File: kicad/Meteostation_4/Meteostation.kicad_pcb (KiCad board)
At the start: 2 copper layers, 45 x 45 mm, 105 parts, among them J1 TxD, J10 GM+, J11 GM-, J12 SWD, J13 SWC, J2 RxD, J3 BME280_SCL, J4 BME280_SDA, J5 RST, J6 +EXT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

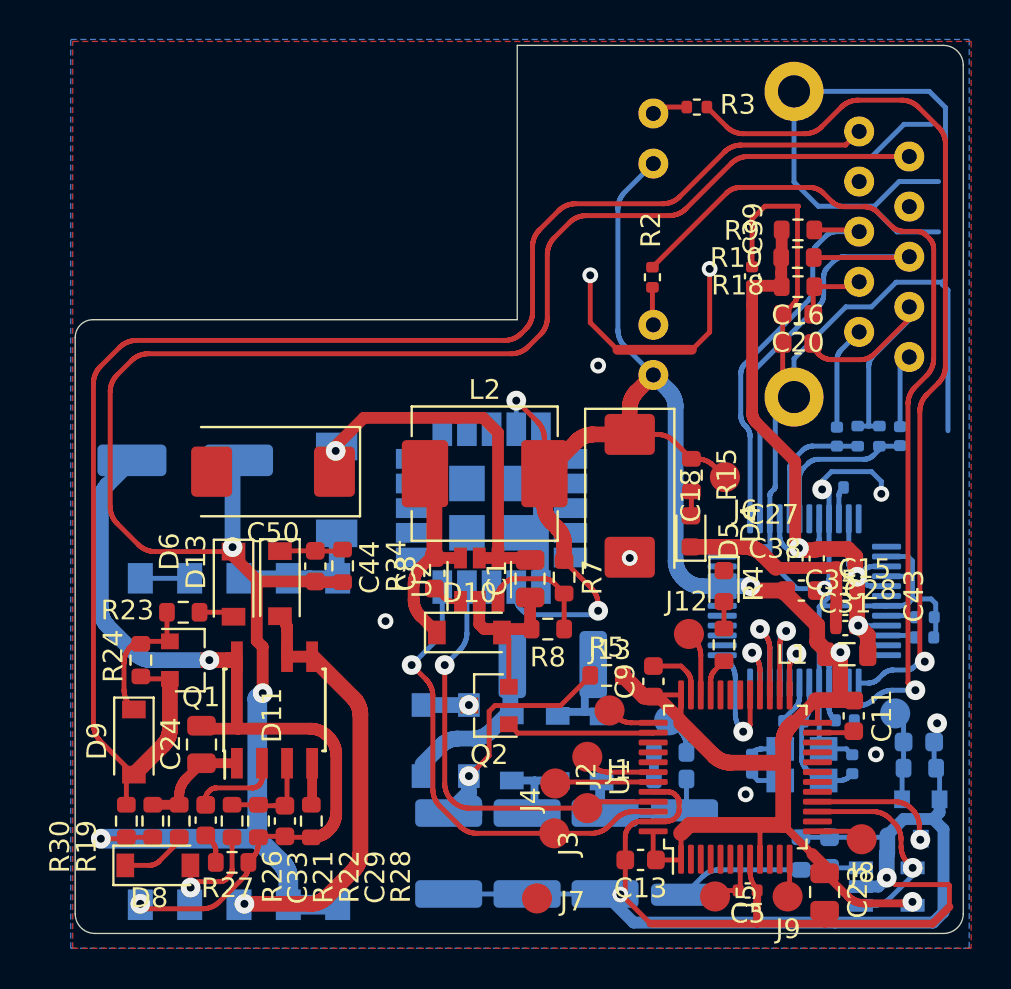
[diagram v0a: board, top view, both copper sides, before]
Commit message: новый файл:    Documents/5N10.pdf 	изменено:      kicad/Meteostation_4/Meteostation.kicad_pcb 	изменено:      kicad/Meteostation_4/Meteostation.kicad_pcb-bak 	изменено:      kicad/Meteostation_4/Meteostation.sch 	изменено:      kicad/Meteostation_4/Meteostation.sch-bak 	изменено:      kicad/Meteostation_4/fp-info-cache
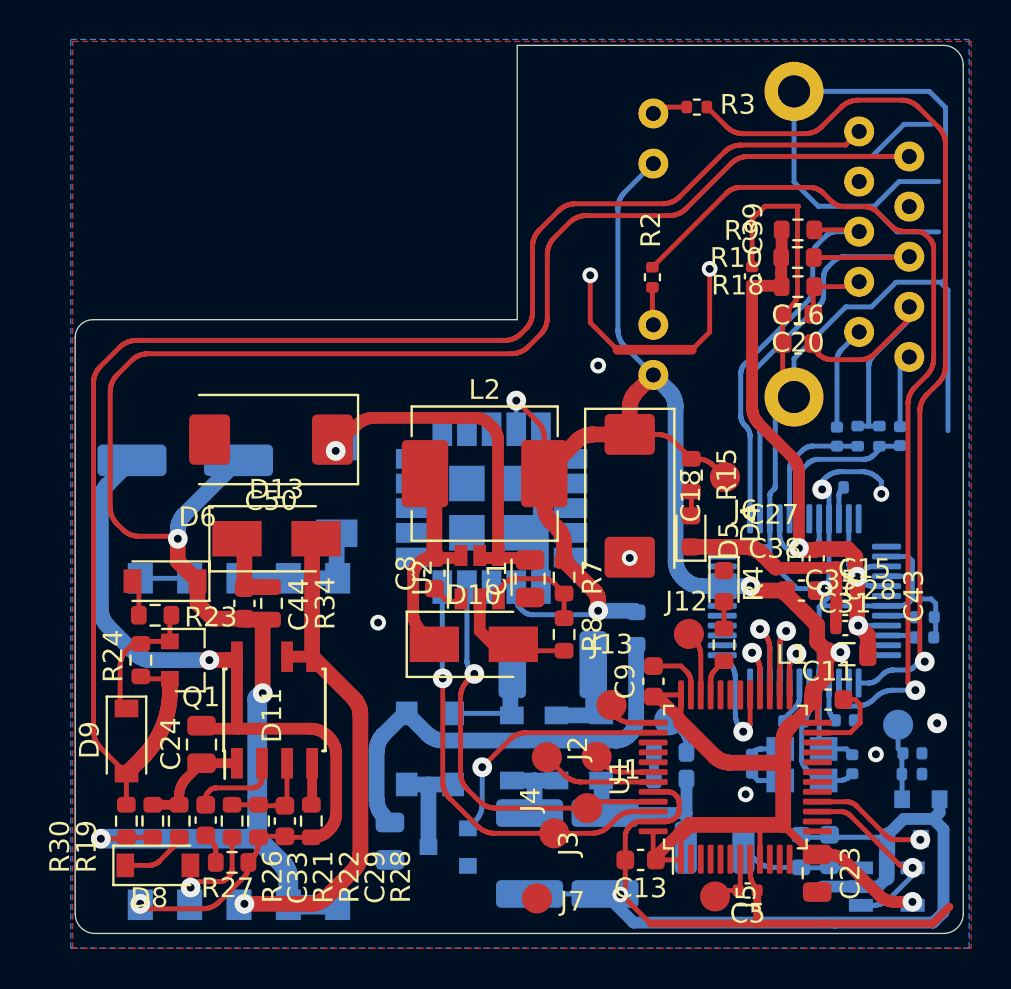
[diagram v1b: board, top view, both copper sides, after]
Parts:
- removed J8: RxD_AirS8(D8), My-library:SMD-CONN
- removed J9: TxD_AirS8(D9), My-library:SMD-CONN
- C2: footprint Capacitor_SMD:C_1812_4532Metric -> Capacitor_SMD:C_0805_2012Metric
- C21: value 15pF -> 200; footprint Capacitor_SMD:C_0603_1608Metric -> Capacitor_SMD:C_0402_1005Metric
- C22: value 15pF -> 100
- C8: value 480p -> 150nF
- D10: value MBR0540 -> RS1M; footprint Diode_SMD:D_SOD-123 -> Diode_SMD:D_SMA
- D13: footprint Diode_SMD:D_SOD-123 -> Diode_SMD:D_SMA
- Q2, R5: moved to B.Cu
- R13: footprint Resistor_SMD:R_1812_4532Metric -> Resistor_SMD:R_1210_3225Metric
- R25: footprint Resistor_SMD:R_0603_1608Metric -> Resistor_SMD:R_0402_1005Metric
- R7: value 10k -> 3.4k
- R8: value 10k -> 1.02k
- moved Q2 7.47 mm to (38.0, 100.5)
- moved R34 4.07 mm to (29.1, 88.2)
- moved C44 4.06 mm to (27.7, 88.2)
- moved D6 3.48 mm to (23.6, 87.0), turned to 180 degrees
- moved C2 3.04 mm to (35.0, 100.2)
- moved R5 2.81 mm to (47.5, 89.5), turned to 90 degrees
- moved D13 2.28 mm to (29.3, 84.9), turned to 0 degrees
- moved C50 1.63 mm to (29.0, 79.9)
- moved R13 1.55 mm to (51.5, 100.5), turned to 0 degrees
- moved C11 1.54 mm to (57.2, 93.0), turned to 0 degrees
- moved R23 1.43 mm to (23.1, 88.8), turned to 180 degrees
- moved J2 1.39 mm to (43.0, 96.0)
- moved C23 1.02 mm to (56.7, 101.8)
- moved D1 0.91 mm to (37.1, 95.5), turned to 0 degrees
- moved R8 0.87 mm to (43.9, 89.8), turned to 270 degrees
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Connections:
- U1 pad 12: Net-(J9-Pad1) -> (no net)
- U1 pad 13: Net-(J8-Pad1) -> (no net)
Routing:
- net Net-(C2-Pad1): track 12.5 -> 23.0 mm, vias 1 -> 0
- net GND: track 253.6 -> 243.8 mm, vias 13 -> 12
- net PWR: track 7.52 -> 12.7 mm, vias 0 -> 1
- net Net-(D11-Pad5): track 21.5 -> 25.4 mm
- net Net-(D1-Pad2): track 2.35 -> 5.54 mm, vias 1 -> 0
- net Net-(C22-Pad2): track 9.61 -> 6.52 mm
- net Net-(C19-Pad1): track 102.2 -> 99.6 mm
- net Net-(C3-Pad2): track 8.23 -> 5.79 mm
- net Net-(J8-Pad1): track 2.40 -> 0.00 mm
- net Net-(C17-Pad1): track 7.42 -> 9.52 mm
- net Net-(J9-Pad1): track 1.93 -> 0.00 mm
- net SDA: track 23.9 -> 22.2 mm
- net 12-16: track 19.4 -> 18.0 mm
- net SCL: track 21.8 -> 20.6 mm
- net Net-(C21-Pad2): track 4.79 -> 3.90 mm
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
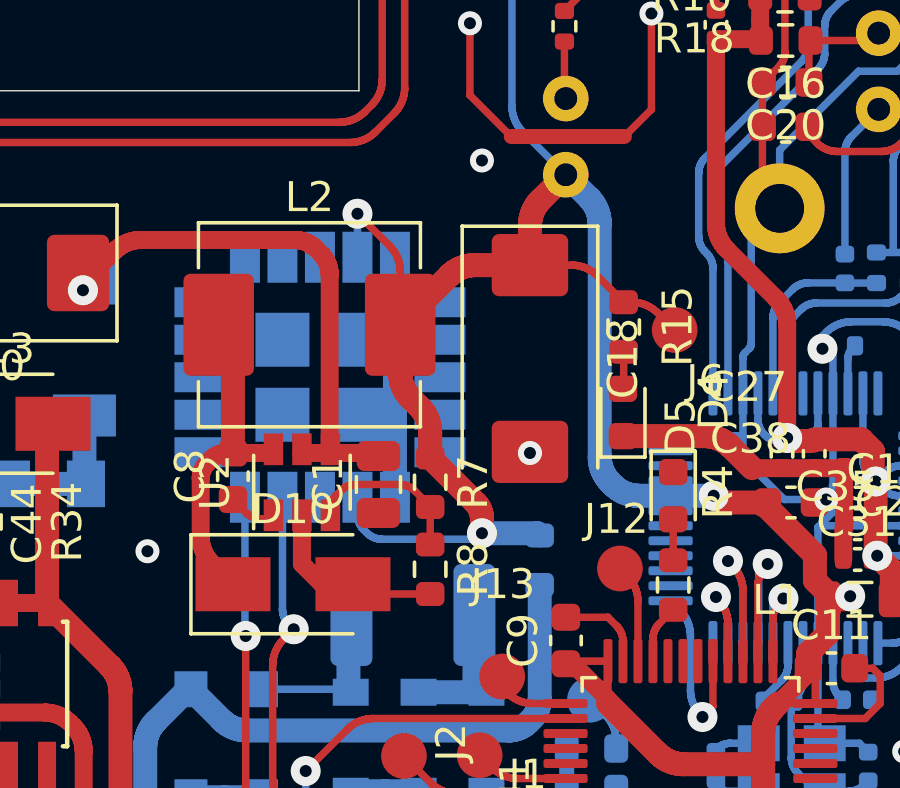
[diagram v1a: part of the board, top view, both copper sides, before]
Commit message: изменено:      kicad/Meteostation_4/Meteostation-cache.lib 	изменено:      kicad/Meteostation_4/Meteostation-rescue.lib 	изменено:      kicad/Meteostation_4/Meteostation.kicad_pcb 	изменено:      kicad/Meteostation_4/Meteostation.kicad_pcb-bak 	изменено:      kicad/Meteostation_4/Meteostation.sch 	изменено:      kicad/Meteostation_4/Meteostation.sch-bak
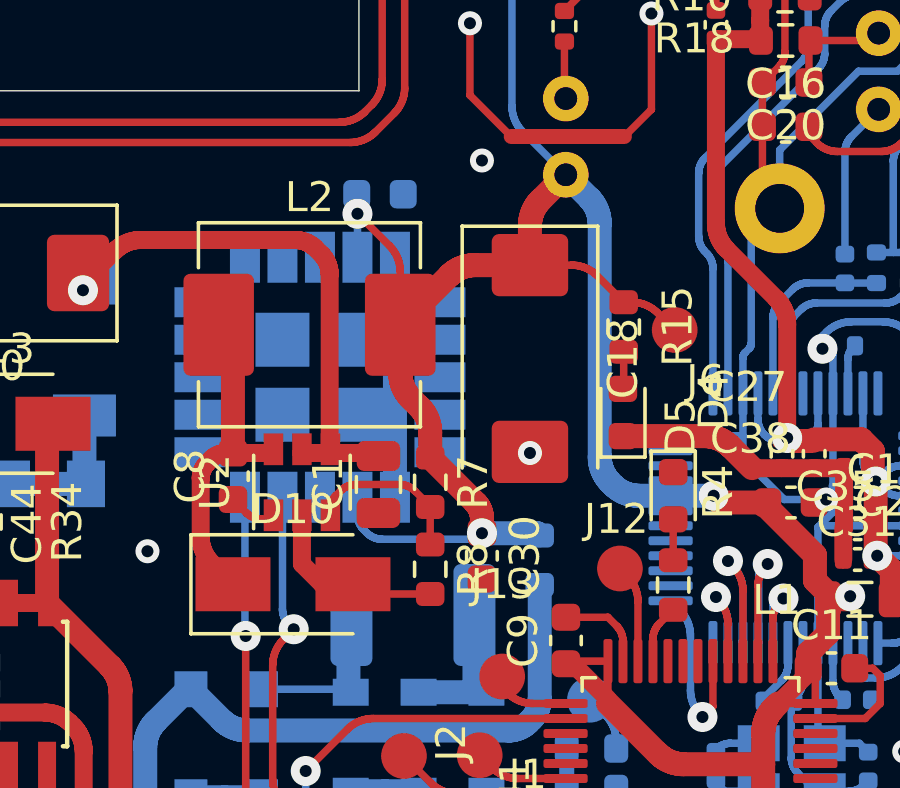
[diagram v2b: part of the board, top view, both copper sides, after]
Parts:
- added C30: 0.1uF, Capacitor_SMD:C_0603_1608Metric, F.Cu at (45.6, 89.3)
- added C32: 0.1uF, Capacitor_SMD:C_0603_1608Metric, B.Cu at (42.2, 77.2)
- D1: value B82801A1 -> B82801A150
- Y2: value ECS-250-20-33 -> ECS-250-20-33 25MHz
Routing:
- net +3.3VDAC: track 117.2 -> 117.9 mm

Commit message: изменено:      kicad/Meteostation_4/Meteostation.kicad_pcb
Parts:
- moved C32 3.10 mm to (39.1, 77.2), turned to 180 degrees
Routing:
- net +3.3VDAC: track 117.9 -> 119.2 mm

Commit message: изменено:      kicad/Meteostation_4/Meteostation.kicad_pcb 	изменено:      kicad/Meteostation_4/Meteostation.kicad_pcb-bak 	изменено:      kicad/Meteostation_4/Meteostation.sch 	изменено:      kicad/Meteostation_4/Meteostation.sch-bak
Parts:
- moved R11 0.29 mm to (57.8, 82.4)
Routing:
- net GND: track 243.8 -> 242.8 mm

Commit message: изменено:      kicad/Meteostation_4/Meteostation.kicad_pcb 	изменено:      kicad/Meteostation_4/Meteostation.kicad_pcb-bak 	изменено:      kicad/Meteostation_4/Meteostation.sch 	изменено:      kicad/Meteostation_4/Meteostation.sch-bak 	изменено:      kicad/Meteostation_4/fp-info-cache 	Documents/ATS-1270R.pdf 	Documents/f1-f7.pdf
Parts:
- D13: value MBR0540 -> F7; footprint Diode_SMD:D_SMA -> Diode_SMD:D_SOD-123F
- D14: value T4932B -> ATS-1270R
- D16: value MBR0540 -> SS36; footprint Diode_SMD:D_SOD-128 -> Diode_SMD:D_SMA
- D8: value MBR0540 -> F7; footprint Diode_SMD:D_SOD-123 -> Diode_SMD:D_SOD-123F
- Q2: value BSS138 -> IRLML6346
- R13: footprint Resistor_SMD:R_1210_3225Metric -> Resistor_SMD:R_1206_3216Metric
- moved D13 3.33 mm to (31.1, 87.7), turned to 270 degrees
- moved D9 2.09 mm to (21.1, 93.2)
- moved D6 2.06 mm to (24.6, 88.8)
- moved R23 1.65 mm to (21.6, 89.3), turned to 90 degrees
- moved Q1 1.35 mm to (24.9, 92.4)
- moved R24 1.32 mm to (22.6, 92.3)
- moved C24 0.29 mm to (25.6, 95.6)
- moved D8 0.19 mm to (23.4, 101.5)
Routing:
- net Net-(D11-Pad5): track 25.4 -> 21.1 mm
- net Net-(D9-Pad2): track 75.6 -> 72.4 mm
- net Net-(D9-Pad1): track 6.91 -> 4.26 mm

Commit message: изменено:      kicad/Meteostation_4/Meteostation.kicad_pcb 	изменено:      kicad/Meteostation_4/Meteostation.kicad_pcb-bak 	изменено:      kicad/Meteostation_4/Meteostation.sch 	изменено:      kicad/Meteostation_4/Meteostation.sch-bak 	изменено:      kicad/Meteostation_4/fp-info-cache
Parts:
- C2, Q2: moved to F.Cu
- D10: value RS1M -> SS56
- D13, D8: value F7 -> FR107W F7
- R5: value 10 -> 47; moved to F.Cu
- moved C2 6.61 mm to (38.4, 94.5), turned to 0 degrees
- moved R5 5.88 mm to (42.2, 92.0), turned to 0 degrees
- moved D10 5.88 mm to (34.4, 87.0), turned to 270 degrees
- moved Q2 3.44 mm to (38.7, 97.2), turned to 270 degrees
- moved C18 3.01 mm to (47.7, 85.7)
- moved J6 2.97 mm to (49.4, 80.4)
- moved C30 2.93 mm to (43.0, 90.7), turned to 180 degrees
- moved R17 2.53 mm to (49.1, 99.6), turned to 270 degrees
- moved D6 2.40 mm to (23.2, 86.9)
- moved C3 1.90 mm to (44.9, 92.3)
- moved D5 1.77 mm to (52.0, 84.0)
- moved D2 1.75 mm to (42.7, 96.5)
- moved D1 1.70 mm to (38.6, 96.2)
- moved D7 1.68 mm to (44.9, 96.5)
- moved R13 1.67 mm to (52.8, 101.6)
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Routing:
- net Net-(C2-Pad1): track 23.0 -> 5.73 mm, vias 0 -> 1
- net SCL: track 20.6 -> 25.5 mm
- net PWR: track 12.7 -> 9.25 mm, vias 1 -> 0
- net SDA: track 22.2 -> 25.5 mm
- net Net-(D1-Pad2): track 5.54 -> 2.35 mm, vias 0 -> 1
- net Net-(C17-Pad1): track 9.52 -> 6.89 mm
- net Net-(C8-Pad2): track 11.3 -> 8.72 mm
- net GND: track 242.8 -> 245.2 mm, vias 12 -> 14
- net Net-(C22-Pad2): track 6.52 -> 4.87 mm
- net +3.3VDAC: track 119.2 -> 120.3 mm
- net 12-16: track 18.0 -> 17.0 mm

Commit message: изменено:      kicad/Meteostation_4/Meteostation.kicad_pcb 	изменено:      kicad/Meteostation_4/Meteostation.kicad_pcb-bak 	изменено:      kicad/Meteostation_4/Meteostation.sch 	изменено:      kicad/Meteostation_4/Meteostation.sch-bak
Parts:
- removed J5: RST, My-library:SMD-CONN
- added R6: 100k, Resistor_SMD:R_0603_1608Metric, F.Cu at (42.5, 94.6)
- moved R16 4.65 mm to (51.6, 99.1)
- moved C22 4.54 mm to (53.0, 99.2)
- moved U3 4.43 mm to (55.9, 101.5)
- moved R13 2.21 mm to (50.6, 101.8)
- moved C2 1.87 mm to (40.1, 93.8)
- moved Q3 1.69 mm to (60.3, 98.8), turned to 180 degrees
- moved Q2 1.69 mm to (40.2, 96.4)
- moved R23 1.68 mm to (23.1, 90.0), turned to 180 degrees
- moved D6 1.38 mm to (23.2, 88.3)
- moved J2 1.29 mm to (44.3, 96.0)
- moved C16 1.20 mm to (54.5, 74.9)
- moved C20 1.20 mm to (54.5, 73.5)
- moved R10 1.20 mm to (54.5, 70.6)
- moved R18 1.20 mm to (54.5, 72.0)
- moved R9 1.20 mm to (54.5, 69.2)
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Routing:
- net GND: track 245.2 -> 167.0 mm, vias 14 -> 12
- net Net-(C19-Pad1): track 99.8 -> 93.8 mm
- net Net-(D9-Pad2): track 72.3 -> 77.7 mm
- net Net-(D3-Pad25): track 44.6 -> 41.0 mm
- net +3.3VDAC: track 120.3 -> 117.5 mm
- net Pulse: track 5.95 -> 3.17 mm
- net Net-(C2-Pad1): track 5.73 -> 3.11 mm
- net Net-(D3-Pad2): track 23.5 -> 25.9 mm
- net Net-(D3-Pad27): track 45.2 -> 47.5 mm
- net Net-(D3-Pad1): track 20.2 -> 22.2 mm
- net PWR: track 9.25 -> 7.47 mm
- net Net-(C5-Pad2): track 2.97 -> 1.56 mm
- net Net-(J2-Pad1): track 5.85 -> 4.57 mm
- net Net-(C17-Pad1): track 6.89 -> 5.92 mm
- net Net-(C20-Pad1): track 3.80 -> 4.65 mm
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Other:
- board size 45 x 45 mm -> 44 x 44 mm

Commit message: изменено:      kicad/Meteostation_4/Meteostation.kicad_pcb 	изменено:      kicad/Meteostation_4/Meteostation.kicad_pcb-bak 	изменено:      kicad/Meteostation_4/Meteostation.sch 	изменено:      kicad/Meteostation_4/Meteostation.sch-bak 	изменено:      kicad/Meteostation_4/fp-info-cache
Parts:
- J1, J12, J13, J2: footprint My-library:SMD-CONN -> My-library:ConnMini
- moved R3 1.17 mm to (50.5, 64.4), turned to 270 degrees
- moved C32 1.09 mm to (39.3, 78.3)
- moved D15 0.78 mm to (40.2, 84.1)
- moved R2 0.32 mm to (48.0, 71.7)
- moved C3 0.29 mm to (44.9, 92.3)
- moved L2 0.25 mm to (40.1, 81.5)
- moved D4 0.17 mm to (52.0, 87.5)
- moved D12 0.12 mm to (47.1, 96.3)
- moved D2 0.12 mm to (42.7, 96.3)
- moved D7 0.12 mm to (44.9, 96.3)
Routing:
- net GND: track 167.0 -> 189.9 mm
- net +3.3VDAC: track 117.5 -> 115.0 mm
- net Net-(D3-Pad1): track 22.2 -> 20.8 mm
- net Net-(D3-Pad2): track 25.9 -> 24.5 mm
- net SCL: track 25.4 -> 24.4 mm
- net Net-(C17-Pad1): track 5.92 -> 6.74 mm
- net SDA: track 25.5 -> 24.8 mm
- net Net-(C3-Pad2): track 5.29 -> 4.57 mm
- net Net-(D3-Pad25): track 41.0 -> 40.4 mm
- net Link: track 2.06 -> 2.64 mm
